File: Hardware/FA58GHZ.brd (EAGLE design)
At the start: 41.9 x 24.1 mm, 51 parts, among them IC1 MAX4311EEE, IC2 MCP6001, IC3 MCP6001, Q2 pchanel, Q3 200mA/50V, U1 ATMEGA328P_TQFP, U2 RX5808, X1 SMA-SMDPCB, Y1 16MHZ

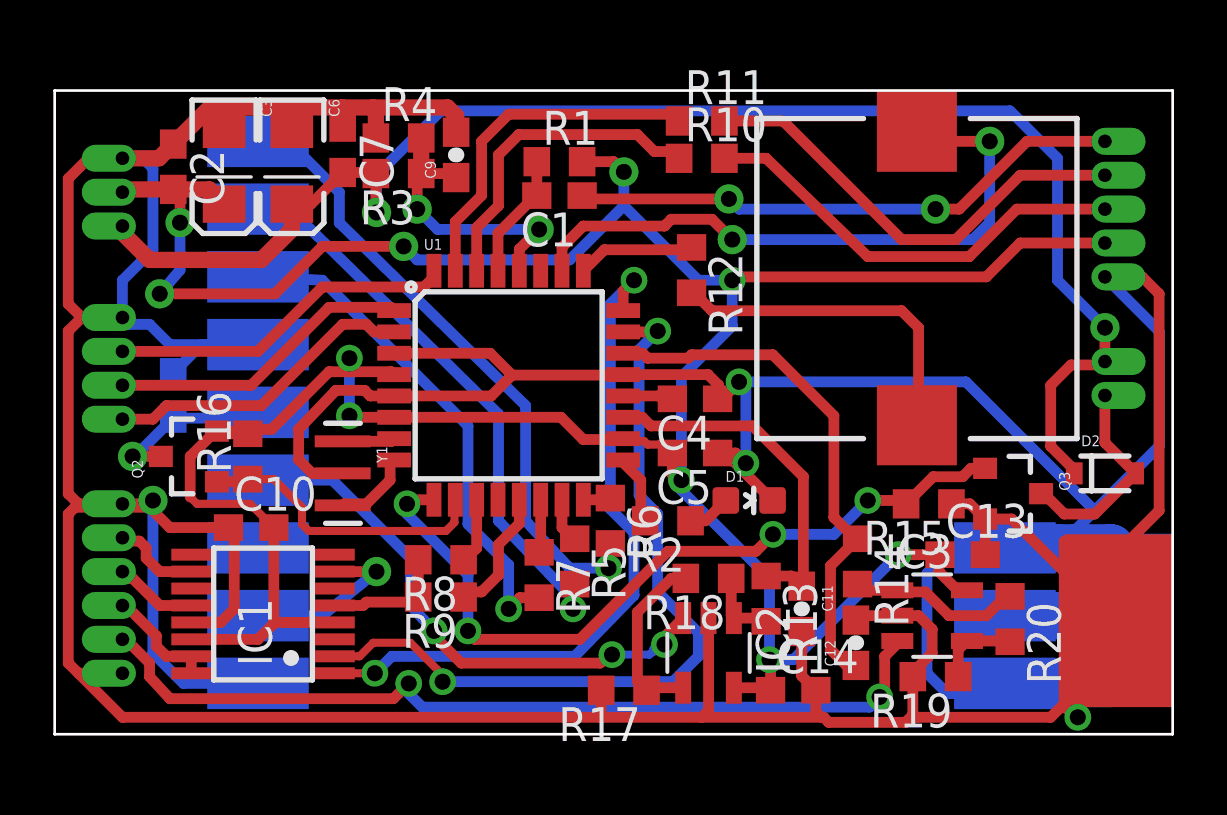
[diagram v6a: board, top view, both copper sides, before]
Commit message: BOARD VER: 1.1 - Fix footprints and pinout problems with RF
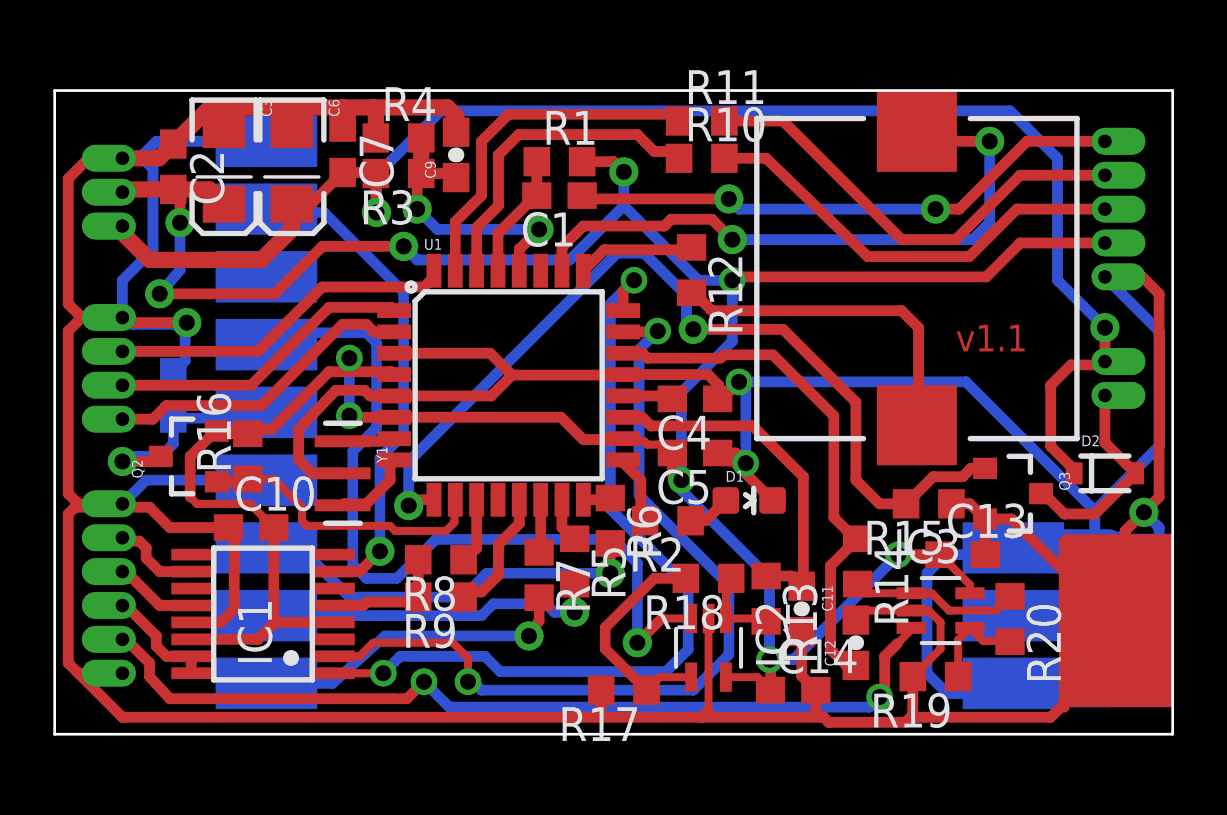
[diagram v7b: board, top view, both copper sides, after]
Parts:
- IC1: device maxim:QSOP16 -> FreakyAttic-EagleLibrary:QSOP16
- IC2, IC3: device linear:SOT23-5 -> FreakyAttic-EagleLibrary:SC70-5
- X1: value SMA-SMDPCB -> SMA
- moved IC3 0.37 mm to (33.2, 4.64)
- moved U2 0.32 mm to (7.94, 1.91)
- moved IC2 0.19 mm to (24.5, 3.24)
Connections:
- net CLOCK: now also U2.P$7; no longer U2.P$9
- net DATA: now also U2.P$9; no longer U2.P$7
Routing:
- net VIDEO1: track 6.60 -> 18.5 mm
- net RSSI1: track 21.5 -> 30.4 mm, vias 3 -> 1
- net CLOCK: track 23.9 -> 15.1 mm
- net SELECT: track 21.5 -> 12.9 mm
- net DATA: track 18.9 -> 12.2 mm
- net FAN: track 29.1 -> 34.3 mm, vias 4 -> 2
- net SEL1: track 26.4 -> 31.2 mm
- net GND: track 251.2 -> 255.0 mm
- net SEL0: track 29.7 -> 31.9 mm
- net N$14: track 6.82 -> 8.78 mm
- net N$20: track 6.44 -> 8.25 mm
- net N$15: track 3.10 -> 3.73 mm
- net AN_RSSI1: track 2.79 -> 3.32 mm
- net VCC: track 120.4 -> 120.9 mm
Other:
- board text added: "v1.1"
